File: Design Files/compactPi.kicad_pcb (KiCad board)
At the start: 6 copper layers, 47 x 105 mm, 143 parts, among them J1 1053101208, J10 Conn_01x06_MountingPin, J11 Conn_01x04_MountingPin, J12 Conn_01x02_MountingPin, J13 Conn_01x02_MountingPin, J14 Micro_SD_Card_Det, J15 USB_C_Receptacle_USB2.0, J16 Conn_01x06_MountingPin, J17 Conn_01x06_MountingPin, J18 Conn_01x06_MountingPin, J19 Conn_01x06_MountingPin, J2 HDMI_A_1.4, J3 Conn_01x04_MountingPin, J4 Conn_01x06_MountingPin, J5 Conn_01x04_MountingPin, J6 Conn_01x04_MountingPin, J7 Conn_01x04_MountingPin, J8 Conn_01x04_MountingPin, J9 Conn_01x04_MountingPin, U1 RT9742GGJ5, U10 BMI270, U11 74LVC2T45DC, U12 74LVC2T45DC, U13 TLVM13630RDHR, U14 TLVM13630RDHR, U15 AK09918C, U16 74LVC2T45DC, U17 RT9742SNGV, U18 PCA9685PW, U19 74LVC2T45DC, U2 AT24CS64-MAHM, U20 MMC5983MA, U21 MCP25625x-x-ML, U22 WE-TVS-82400102, U23 WE-TVS-82400102, U24 TCA9517ADGK, U25 BMP390, U4 LM74700QDBVRQ1, U5 CSD18511Q5A, U6 CSD18511Q5A, U7 LM74700QDBVRQ1, U8 CSD18511Q5A, U9 LM74700QDBVRQ1, Y1 Crystal_GND24_Small

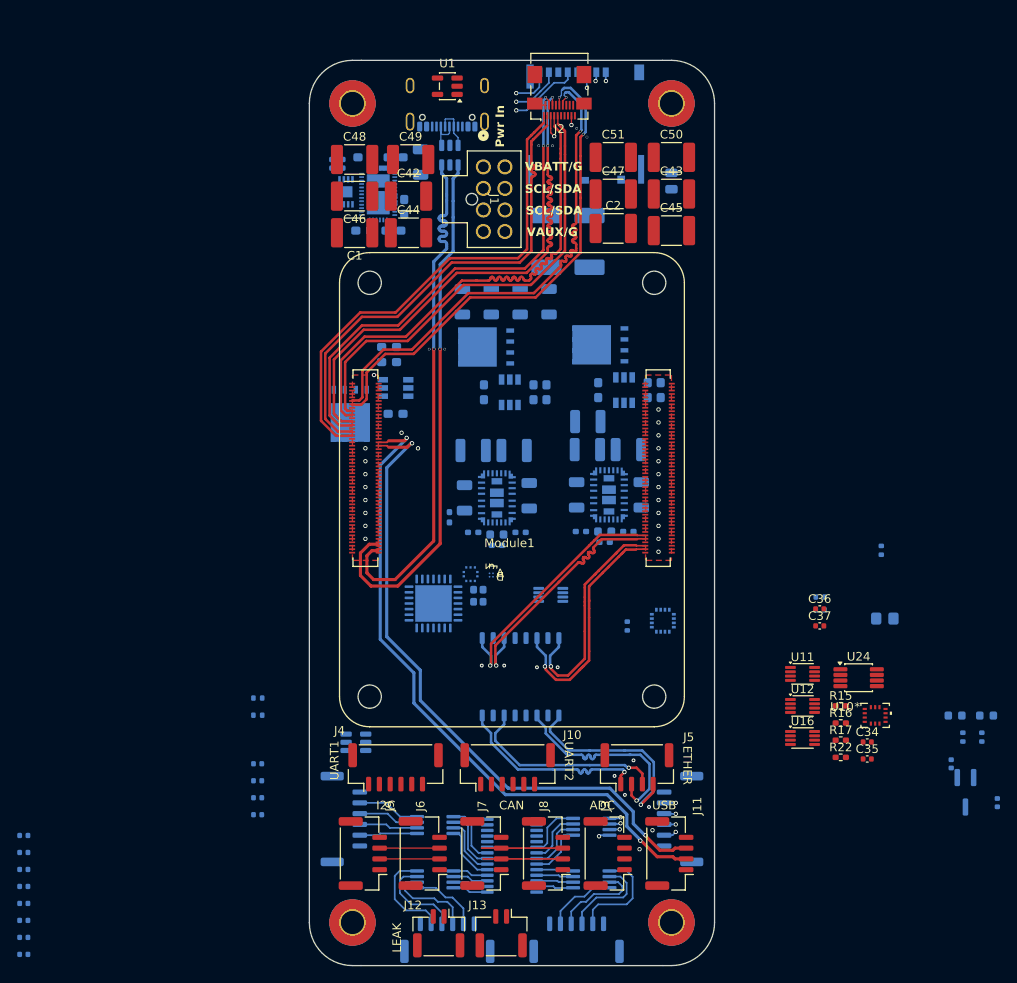
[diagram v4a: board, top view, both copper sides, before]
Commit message: Additional layout updates
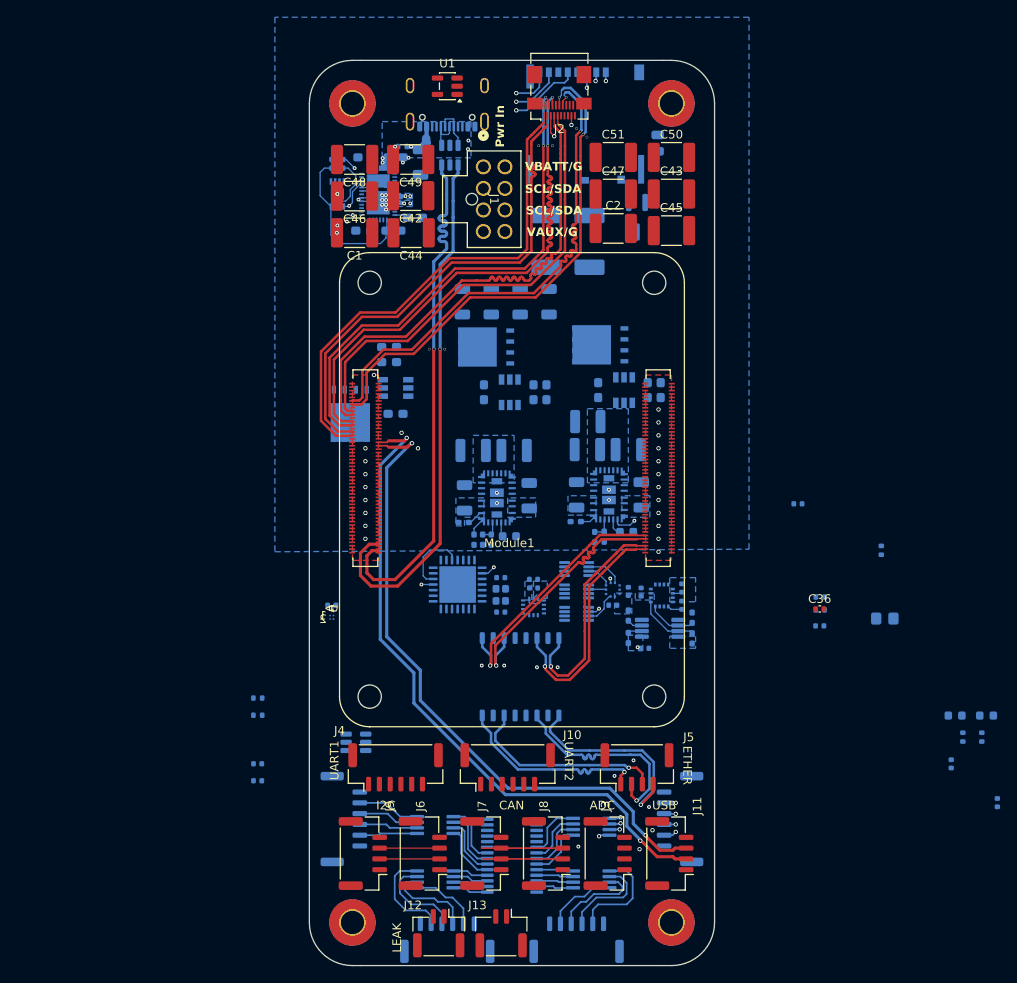
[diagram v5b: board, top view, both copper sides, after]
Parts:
- removed U19: 74LVC2T45DC, Package_SO:VSSOP-8_2.3x2mm_P0.5mm
- C34, C35, C37, R15, R16, R17, R22, U10, U11, U12, U16, U24: moved to B.Cu
- R10, R13: value R_US -> 53.6k
- R11, R14, R8: value R_US -> 10k
- R7, R9: value R_US -> 25.5k
- moved C63 81.5 mm to (144.7, 105.9), turned to 90 degrees
- moved C62 81.5 mm to (144.7, 107.9), turned to 90 degrees
- moved C57 80.8 mm to (138.5, 106.3), turned to 90 degrees
- moved C61 78.5 mm to (140.0, 106.4), turned to 90 degrees
- moved C58 77.5 mm to (136.7, 107.9), turned to 180 degrees
- moved U17 76.8 mm to (139.5, 62.9)
- moved C59 69.5 mm to (127.5, 105.9)
- moved C60 69.0 mm to (127.5, 104.9)
- moved R12 61.4 mm to (112.3, 54.7), turned to 180 degrees
- moved C55 54.0 mm to (104.1, 107.9), turned to 180 degrees
- moved U10 41.6 mm to (127.5, 108.1)
- moved C52 39.4 mm to (123.7, 104.7), turned to 180 degrees
- moved C53 35.5 mm to (123.7, 108.7)
- moved U16 32.7 mm to (132.5, 103.7)
- moved C35 30.7 mm to (158.2, 96.1)
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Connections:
- net Net-(U13-VLDOIN) renamed /Power/5V0_C_RAW
- net Net-(U14-VLDOIN) renamed /Power/5V0_P_RAW
- net Net-(U20-VDDIO) renamed /Autopilot Sensors/MAG_VDDIO
- net Net-(U3-DRAIN_PAD) renamed /Power/USB_DRAIN
- net Net-(U3-LDO_1V5) renamed /Power/LDO_1V5
- net Net-(U3-VIN_3V3) renamed /Power/VIN_3V3
- C19 pad 1: GND -> /Power/V_COMMON
- C21 pad 1: GND -> /Power/V_COMMON
- C26 pad 1: GND -> /Power/V_COMMON
- C28 pad 1: GND -> /Power/V_COMMON
- C30 pad 1: GND -> /Power/V_COMMON
- C31 pad 1: GND -> /Power/V_COMMON
- C33 pad 1: GND -> /Power/V_COMMON
- R14 pad 1: GND -> /Power/V_COMMON
- U10 pad 4: /Autopilot Sensors/INT_IMU1_1V8 -> unconnected-(U10-INT1-Pad4)
- U10 pad 9: /Autopilot Sensors/INT_IMU2_1V8 -> unconnected-(U10-INT2-Pad9)
- U13 pad 18: GND -> /Power/V_COMMON
- U13 pad 19: GND -> /Power/V_COMMON
- U13 pad 26: unconnected-(U13-PG-Pad26) -> GND
- U13 pad 3: GND -> /Power/V_COMMON
- U13 pad 4: GND -> /Power/V_COMMON
- U14 pad 18: GND -> /Power/V_COMMON
- U14 pad 19: GND -> /Power/V_COMMON
- U14 pad 3: GND -> /Power/V_COMMON
- U14 pad 4: GND -> /Power/V_COMMON
- U4 pad 4: GND -> /Power/V_COMMON
- U5 pad 5: GND -> /Power/V_COMMON
- U5 pad 6: GND -> /Power/V_COMMON
- U5 pad 7: GND -> /Power/V_COMMON
- U5 pad 8: GND -> /Power/V_COMMON
- U5 pad 9: GND -> /Power/V_COMMON
- U6 pad 5: GND -> /Power/V_COMMON
- U6 pad 6: GND -> /Power/V_COMMON
- U6 pad 7: GND -> /Power/V_COMMON
- U6 pad 8: GND -> /Power/V_COMMON
- U6 pad 9: GND -> /Power/V_COMMON
- U7 pad 4: GND -> /Power/V_COMMON
- U8 pad 5: GND -> /Power/V_COMMON
- U8 pad 6: GND -> /Power/V_COMMON
- U8 pad 7: GND -> /Power/V_COMMON
- U8 pad 8: GND -> /Power/V_COMMON
- U8 pad 9: GND -> /Power/V_COMMON
- U9 pad 4: GND -> /Power/V_COMMON
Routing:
- net /Power/USB_LDO_3V3: track 0.00 -> 19.6 mm
- net Net-(U21-T_{XD}): track 0.00 -> 12.2 mm, vias 0 -> 2
- net /Power/I2Cc_SDA: track 0.00 -> 10.3 mm, vias 0 -> 2
- net GND: track 4.94 -> 14.7 mm, vias 41 -> 61
- net Net-(U21-R_{XD}): track 0.00 -> 8.03 mm
- net /Power/I2Cc_SCL: track 0.00 -> 7.45 mm
- net /I2C_INT_SCL0: track 0.00 -> 7.10 mm
- net /VBUS: track 0.00 -> 6.96 mm, vias 0 -> 7
- net /Autopilot Sensors/CS_PRES_1V8: track 0.00 -> 6.50 mm, vias 0 -> 2
- net /I2C_INT_SDA0: track 0.00 -> 5.64 mm
- net /Power/USB_DRAIN: track 0.00 -> 4.48 mm
- net /Autopilot Sensors/INT_PRES_1V8: track 0.00 -> 4.27 mm
- net /Autopilot Sensors/SPI_SCK_1V8: track 0.00 -> 3.96 mm
- net /Autopilot Sensors/SPI_CIPO_1V8: track 0.00 -> 2.98 mm
- net /Power/5V0_P_RAW: track 0.00 -> 2.72 mm, vias 0 -> 1
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- added copper zone on B.Cu, net /1V8
- added copper zone on B.Cu, net /3V3
- added copper zone on B.Cu, net /5V0_PERIPHERAL
- added copper zone on B.Cu, net /Power/5V0_C_RAW
- added copper zone on B.Cu, net /Power/5V0_P_RAW
- added copper zone on B.Cu, net /Power/V_COMMON
- added copper zone on B.Cu, net /VBUS
- added copper zone on In3.Cu, net /VBUS
- added copper zone on B.Cu, net GND
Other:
- board text removed: "3V3_S"
- board text removed: "5V0_C"
- board text removed: "5V0_P"

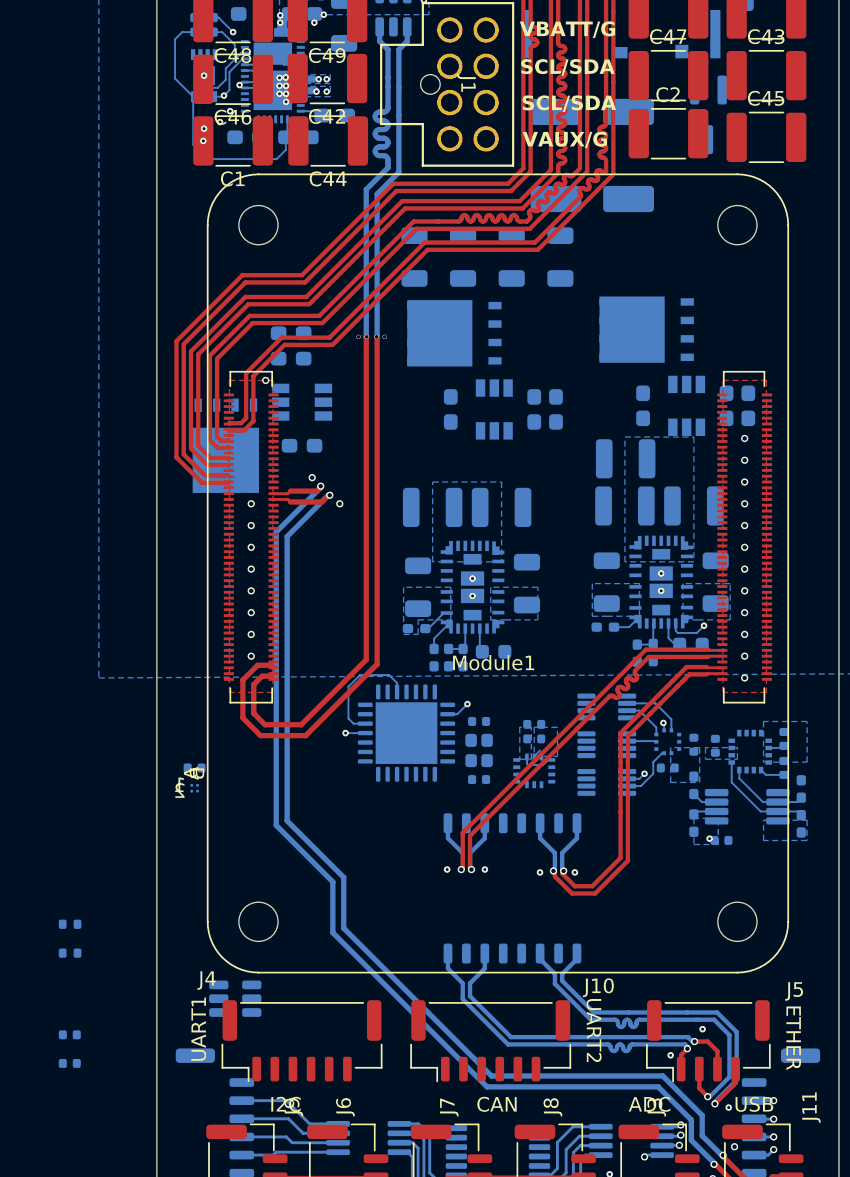
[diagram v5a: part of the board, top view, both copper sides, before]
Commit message: Provisional CAN interface design/layout. Probably need to move more north
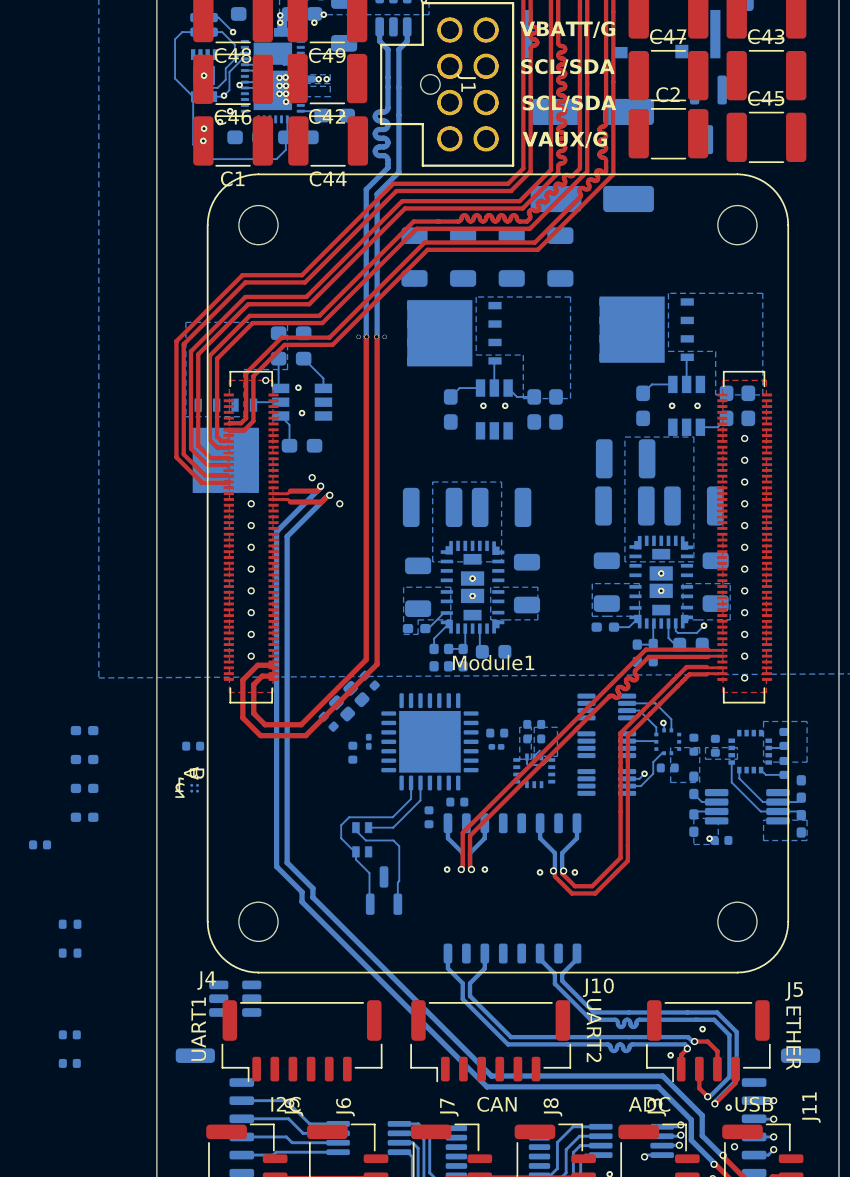
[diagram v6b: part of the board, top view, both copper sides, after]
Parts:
- added C38: 100nF, Capacitor_SMD:C_0402_1005Metric, B.Cu at (120.2, 111.3)
- added C39: 100nF, Capacitor_SMD:C_0402_1005Metric, B.Cu at (122.2, 110.2)
- added C64: 100nF, Capacitor_SMD:C_0402_1005Metric, B.Cu at (125.0, 105.5)
- added C65: 100nF, Capacitor_SMD:C_0402_1005Metric, B.Cu at (115.0, 106.8)
- added C66: 10u, Capacitor_SMD:C_0201_0603Metric, B.Cu at (116.1, 106.1)
- added C67: 10u, Capacitor_SMD:C_0201_0603Metric, B.Cu at (124.9, 106.5)
- added C68: 47pF, Capacitor_SMD:C_0402_1005Metric, B.Cu at (93.5, 113.2)
- added D5: SZNUP2105L, Package_TO_SOT_SMD:SOT-23, B.Cu at (117.2, 116.3)
- added FL1: Choke_CommonMode_FerriteCore_1234, Inductor_SMD:L_CommonModeChoke_Coilcraft_0805USB, B.Cu at (115.7, 112.8)
- added R23: 10k, Resistor_SMD:R_0402_1005Metric_Pad0.72x0.64mm_HandSolder, B.Cu at (96.5, 111.3)
- added R24: 10k, Resistor_SMD:R_0402_1005Metric_Pad0.72x0.64mm_HandSolder, B.Cu at (96.5, 109.3)
- added R25: 120, Resistor_SMD:R_0402_1005Metric_Pad0.72x0.64mm_HandSolder, B.Cu at (96.5, 107.3)
- added R26: 10k, Resistor_SMD:R_0402_1005Metric_Pad0.72x0.64mm_HandSolder, B.Cu at (96.5, 105.3)
- moved C52 10.4 mm to (113.3, 104.7), turned to -45 degrees
- moved C53 10.2 mm to (116.2, 101.9), turned to 135 degrees
- moved Y1 9.57 mm to (114.8, 103.3), turned to 45 degrees
- moved U21 1.72 mm to (120.3, 106.1), turned to 180 degrees
- moved C55 1.50 mm to (104.0, 106.4)
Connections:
- net Net-(U21-OSC1) renamed /Autopilot Interfaces/OSC_1
- net Net-(U21-OSC2) renamed /Autopilot Interfaces/OSC_2
- net Net-(U21-R_{XD}) renamed /Autopilot Interfaces/CAN_RX
- net Net-(U21-T_{XD}) renamed /Autopilot Interfaces/CAN_TX
- U21 pad 12: /Autopilot Interfaces/CAN_L -> /Autopilot Interfaces/CAN_L_PC
- U21 pad 13: /Autopilot Interfaces/CAN_H -> /Autopilot Interfaces/CANH_PC
- U21 pad 15: unconnected-(U21-STBY-Pad15) -> /Autopilot Interfaces/CAN_STBY
- U21 pad 2: unconnected-(U21-~{RESET}-Pad2) -> /Autopilot Interfaces/CAN_RST
- U21 pad 23: unconnected-(U21-~{Rx1BF}-Pad23) -> /Autopilot Interfaces/CAN_PULL_HI
- U21 pad 24: unconnected-(U21-~{Rx0BF}-Pad24) -> /Autopilot Interfaces/CAN_PULL_HI
- U21 pad 6: unconnected-(U21-CLKOUT-Pad6) -> /Autopilot Interfaces/CAN_CLKO
- U21 pad 7: unconnected-(U21-~{Tx0RTS}-Pad7) -> /Autopilot Interfaces/CAN_PULL_HI
- U21 pad 8: unconnected-(U21-~{Tx1RTS}-Pad8) -> /Autopilot Interfaces/CAN_PULL_HI
- U21 pad 9: unconnected-(U21-~{Tx2RTS}-Pad9) -> /Autopilot Interfaces/CAN_PULL_HI
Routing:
- net /Autopilot Interfaces/CANH_PC: track 0.00 -> 13.1 mm
- net /Autopilot Interfaces/CAN_RX: track 8.03 -> 0.00 mm
- net /Autopilot Interfaces/CAN_H: track 9.28 -> 16.9 mm
- net /Power/V_COMMON: track 0.00 -> 6.91 mm
- net /Autopilot Interfaces/CAN_L_PC: track 0.00 -> 5.56 mm
- net /Autopilot Interfaces/CAN_TX: track 12.2 -> 9.23 mm, vias 2 -> 0
- net Net-(U9-VCAP): track 0.00 -> 2.61 mm
- net /Power/V_USB: track 1.21 -> 3.32 mm
- net Net-(U7-VCAP): track 0.00 -> 2.05 mm
- net /Power/V_AUX: track 0.00 -> 2.05 mm
- net Net-(U8-G): track 0.00 -> 1.95 mm
- net Net-(U5-G): track 0.00 -> 1.89 mm
- net Net-(U4-GATE): track 0.00 -> 1.89 mm
- net /Power/5V_PERIPHERAL: track 1.11 -> 0.00 mm
- net GND: vias 61 -> 67
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- added copper zone on B.Cu, net /Power/V_AUX
- added copper zone on B.Cu, net /Power/V_BATT
- added copper zone on B.Cu, net /Power/V_USB

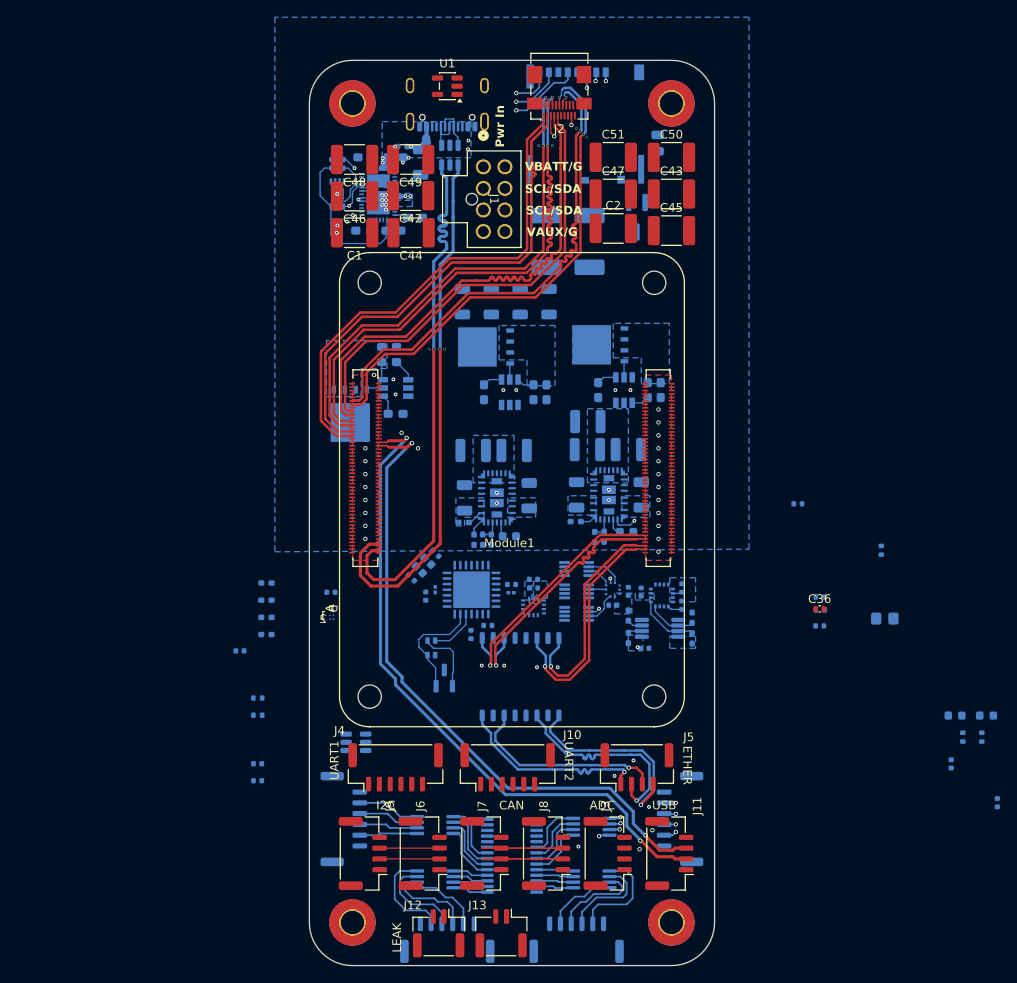
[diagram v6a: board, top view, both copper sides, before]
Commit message: SD pwr routed
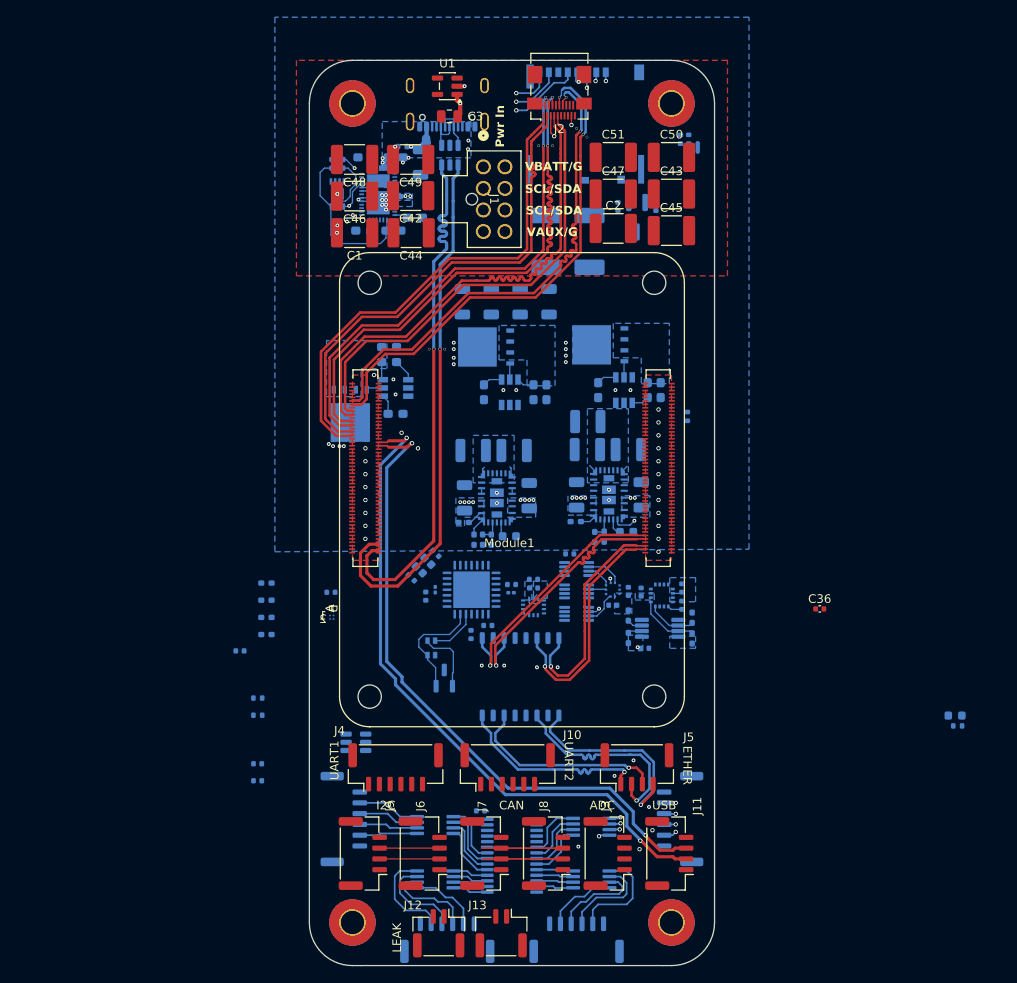
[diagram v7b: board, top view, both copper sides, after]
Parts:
- removed D3: LED Green, LED_SMD:LED_0603_1608Metric
- removed R18: 1k, Resistor_SMD:R_0402_1005Metric
- removed R3: 0R, Resistor_SMD:R_0805_2012Metric_Pad1.20x1.40mm_HandSolder
- added NT1: NetTie_2, NetTie:NetTie-2_SMD_Pad0.5mm, B.Cu at (146.6, 54.8)
- C3: moved to F.Cu
- moved C40 79.7 mm to (141.7, 61.6)
- moved C41 75.3 mm to (137.3, 61.6)
- moved R5 56.7 mm to (145.5, 53.9), turned to 90 degrees
- moved R6 55.5 mm to (144.6, 53.9), turned to 90 degrees
- moved C37 44.8 mm to (121.3, 131.8), turned to 180 degrees
- moved R4 27.3 mm to (145.3, 86.0)
- moved C35 27.1 mm to (131.7, 102.0)
- moved C3 24.3 mm to (117.8, 51.2), turned to 180 degrees
- moved R19 1.43 mm to (176.7, 121.9), turned to 180 degrees
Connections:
- Module1 pad 21: Net-(Module1A-LED_nACT) -> unconnected-(Module1A-LED_nACT-Pad21)
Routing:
- net /CM5 GPIO Ethernet SDIO/SD_PWR: track 0.00 -> 18.8 mm, vias 0 -> 2
- net /Power/5V0_C_RAW: track 0.00 -> 2.22 mm
- net GND: track 14.7 -> 16.9 mm, vias 67 -> 68
- net /Power/5V0_P_RAW: track 2.72 -> 4.77 mm
- net /Power/V_COMMON: vias 0 -> 26
- added copper zone on In3.Cu, net /Power/V_COMMON
